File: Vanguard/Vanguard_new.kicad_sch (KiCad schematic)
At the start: 98 parts, among them J1 USB_C, J2 Conn_02x03_Pin, J3 Micro_SD_Card_Det1, J4 STARBOARD_SERVO, J5 PORTSIDE_SERVO, J6 Conn_01x02_Pin, Q1 BSS138, Q2 BSS138, Q3 BSS138, Q4 BSS138, U1 ATSAMD11D14A-M, U2 ATmega4809-A, U3 AT25DF641A-SH-T, U4 AP2112K-3.3, U5 MPM3610AGQV-P, U6 BNO086, U7 TXB0104D, U8 TPS61092, Y1 32.768kHz

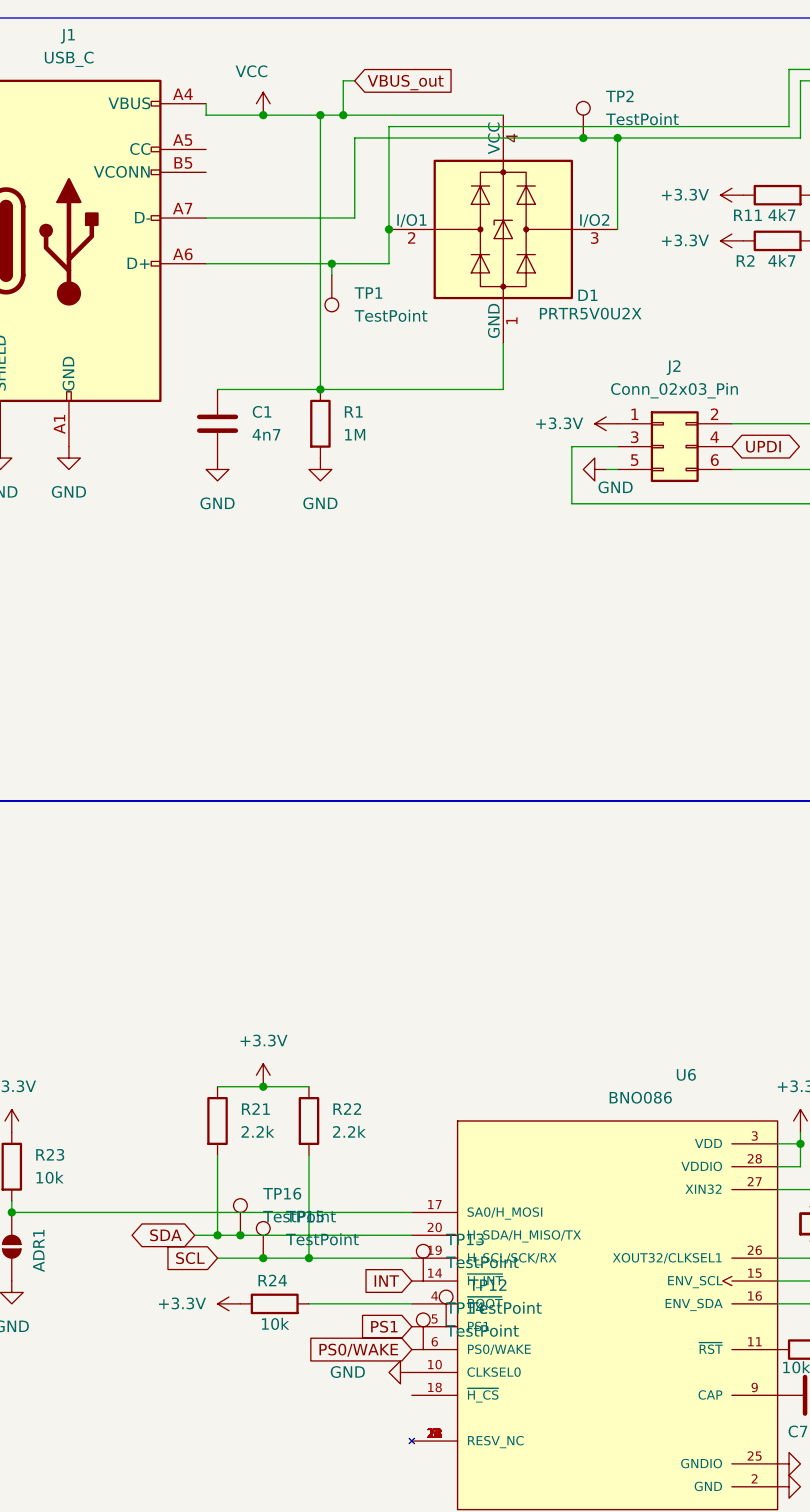
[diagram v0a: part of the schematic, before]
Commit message: slight changes in the original sch. and added a testpoint
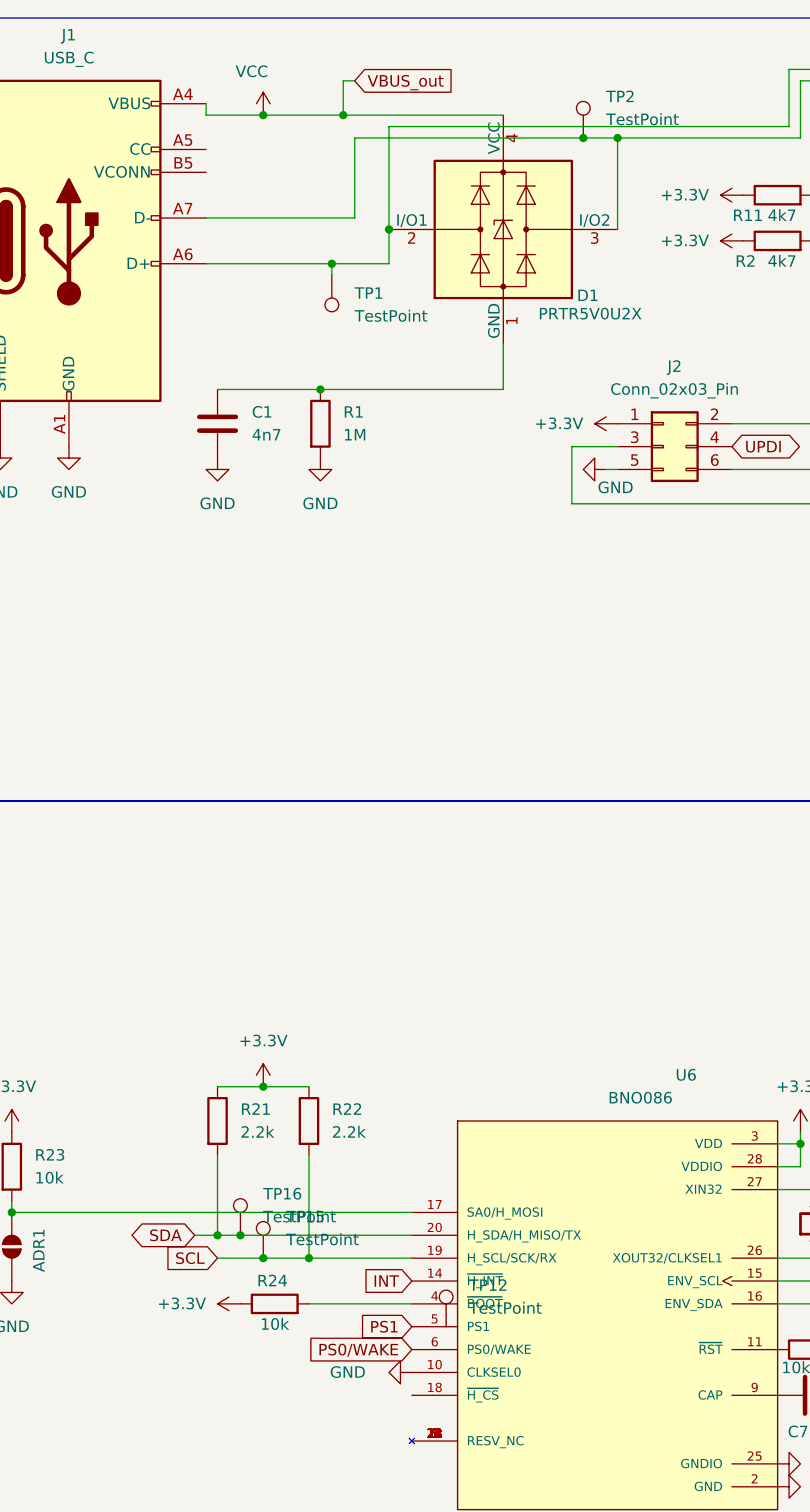
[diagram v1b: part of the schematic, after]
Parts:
- removed TP13, TP14: TestPoint, symbol Connector:TestPoint
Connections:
- net VCC: no longer C1.1, D1.1 (GND), R1.1
- new net: C1.1, D1.1 (GND), R1.1
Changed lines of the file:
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@@
 	)
 	(junction
-		(at 63.5 24.13)
-		(diameter 0)
-		(color 0 0 0 0)
-	)
-	(junction
 		(at 171.45 43.18)
 		(diameter 0)
@@
 	(wire
 		(pts
-			(xy 63.5 54.61) (xy 63.5 24.13)
-		)
-		(stroke
-			(width 0)
-			(type default)
-		)
-	)
-	(wire
-		(pts
 			(xy 53.34 213.36) (xy 62.23 213.36)
 		)
@@
 	(wire
 		(pts
-			(xy 57.15 24.13) (xy 63.5 24.13)
-		)
-		(stroke
-			(width 0)
-			(type default)
-		)
-	)
-	(wire
-		(pts
 			(xy 383.54 185.42) (xy 383.54 182.88)
 		)
@@
 	(wire
 		(pts
-			(xy 63.5 24.13) (xy 66.04 24.13)
+			(xy 57.15 24.13) (xy 66.04 24.13)
 		)
 		(stroke
@@
 	)
 	(symbol
-		(lib_id "Connector:TestPoint")
-		(at 74.93 153.67 0)
-		(unit 1)
-		(exclude_from_sim no)
-		(in_bom yes)
-		(on_board yes)
-		(dnp no)
-		(fields_autoplaced yes)
-		(property "Reference" "TP13"
-			(at 77.47 149.0979 0)
-			(effects
-				(font
-					(size 1.27 1.27)
-				)
-				(justify left)
-			)
-		)
-		(property "Value" "TestPoint"
-			(at 77.47 151.6379 0)
-			(effects
-				(font
-					(size 1.27 1.27)
-				)
-				(justify left)
-			)
-		)
-		(property "Footprint" ""
-			(at 80.01 153.67 0)
-			(effects
-				(font
-					(size 1.27 1.27)
-				)
-				(hide yes)
-			)
-		)
-		(property "Datasheet" "~"
-			(at 80.01 153.67 0)
-			(effects
-				(font
-					(size 1.27 1.27)
-				)
-				(hide yes)
-			)
-		)
-		(property "Description" "test point"
-			(at 74.93 153.67 0)
-			(effects
-				(font
-					(size 1.27 1.27)
-				)
-				(hide yes)
-			)
-		)
-		(pin "1"
-		)
-		(instances
-			(project "Vanguard_new"
-				(path "/972fbf12-2dcd-4fdf-b1c9-8a2880c46640"
-					(reference "TP13")
-					(unit 1)
-				)
-			)
-		)
-	)
-	(symbol
 		(lib_id "Device:R")
 		(at 187.96 35.56 0)
@@
 					(unit 1)
 				)
-			)
-		)
-	)
-	(symbol
-		(lib_id "Connector:TestPoint")
-		(at 74.93 161.29 0)
-		(unit 1)
-		(exclude_from_sim no)
-		(in_bom yes)
-		(on_board yes)
-		(dnp no)
-		(fields_autoplaced yes)
-		(property "Reference" "TP14"
-			(at 77.47 156.7179 0)
-			(effects
-				(font
-					(size 1.27 1.27)
-				)
-				(justify left)
-			)
-		)
-		(property "Value" "TestPoint"
-			(at 77.47 159.2579 0)
-			(effects
-				(font
-					(size 1.27 1.27)
-				)
-				(justify left)
-			)
-		)
-		(property "Footprint" ""
-			(at 80.01 161.29 0)
-			(effects
-				(font
-					(size 1.27 1.27)
-				)
-				(hide yes)
-			)
-		)
-		(property "Datasheet" "~"
-			(at 80.01 161.29 0)
-			(effects
-				(font
-					(size 1.27 1.27)
-				)
-				(hide yes)
-			)
-		)
-		(property "Description" "test point"
-			(at 74.93 161.29 0)
-			(effects
-				(font
-					(size 1.27 1.27)
-				)
-				(hide yes)
-			)
-		)
-		(pin "1"
-		)
-		(instances
-			(project "Vanguard_new"
-				(path "/972fbf12-2dcd-4fdf-b1c9-8a2880c46640"
-					(reference "TP14")
-					(unit 1)
-				)
